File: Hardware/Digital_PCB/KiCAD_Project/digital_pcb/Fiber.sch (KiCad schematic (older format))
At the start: 8 parts, among them Q1 MMBT3904, U6 SN74LVC1G17-EP

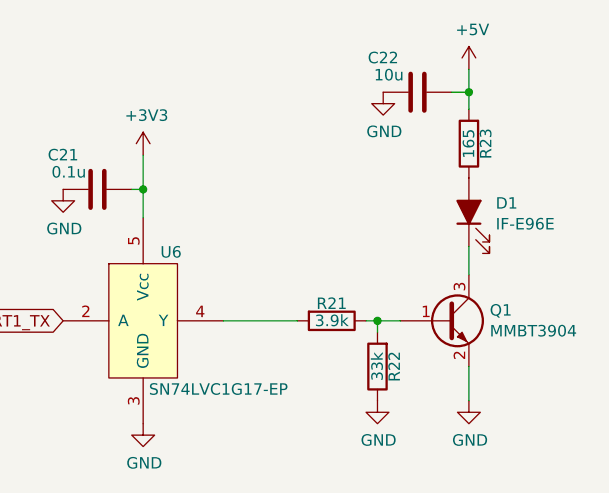
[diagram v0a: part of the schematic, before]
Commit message: Digital PCB Rev 1.0 complete.
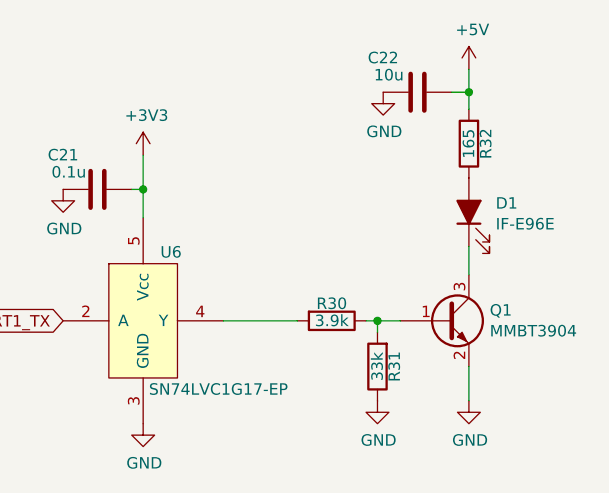
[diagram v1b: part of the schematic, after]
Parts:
- renumbered R21 to R30, R22 to R31, R23 to R32
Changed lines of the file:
@@
 Sheet 4 5
 Title "Digital Rotating Electronics - NSSL EFM"
-Date "2019-11-26"
+Date "2019-12-30"
 Rev "1.0"
 Comp "Leeman Geophysical LLC"
@@
 UART1_TX
 $Comp
-L Device:R R21
+L Device:R R30
 U 1 1 5DECF997
 P 6000 3750
-F 0 "R21" V 5925 3750 50  0000 C CNN
+F 0 "R30" V 5925 3750 50  0000 C CNN
 F 1 "3.9k" V 6000 3750 50  0000 C CNN
 F 2 "Resistors_SMD:R_0603_HandSoldering" V 5930 3750 50  0001 C CNN
@@
 $EndComp
 $Comp
-L Device:R R22
+L Device:R R31
 U 1 1 5DECFEA9
 P 6200 3950
-F 0 "R22" V 6125 3950 50  0000 C CNN
+F 0 "R31" V 6125 3950 50  0000 C CNN
 F 1 "33k" V 6200 3950 50  0000 C CNN
 F 2 "Resistors_SMD:R_0603_HandSoldering" V 6130 3950 50  0001 C CNN
@@
 	6200 3750 6300 3750
 $Comp
-L power:GND #PWR051
+L power:GND #PWR061
 U 1 1 5DED209E
 P 6200 4100
-F 0 "#PWR051" H 6200 3850 50  0001 C CNN
+F 0 "#PWR061" H 6200 3850 50  0001 C CNN
 F 1 "GND" H 6205 3927 50  0000 C CNN
 F 2 "" H 6200 4100 50  0001 C CNN
@@
 $EndComp
 $Comp
-L power:GND #PWR054
+L power:GND #PWR064
 U 1 1 5DED2797
 P 6600 4100
-F 0 "#PWR054" H 6600 3850 50  0001 C CNN
+F 0 "#PWR064" H 6600 3850 50  0001 C CNN
 F 1 "GND" H 6605 3927 50  0000 C CNN
 F 2 "" H 6600 4100 50  0001 C CNN
@@
 	6600 3425 6600 3550
 $Comp
-L Device:R R23
+L Device:R R32
 U 1 1 5DED4330
 P 6600 2975
-F 0 "R23" V 6525 2975 50  0000 C CNN
+F 0 "R32" V 6525 2975 50  0000 C CNN
 F 1 "165" V 6600 2975 50  0000 C CNN
 F 2 "Resistors_SMD:R_0603_HandSoldering" V 6530 2975 50  0001 C CNN
@@
 $EndComp
 $Comp
-L power:+5V #PWR053
+L power:+5V #PWR063
 U 1 1 5DED4F9E
 P 6600 2650
-F 0 "#PWR053" H 6600 2500 50  0001 C CNN
+F 0 "#PWR063" H 6600 2500 50  0001 C CNN
 F 1 "+5V" H 6615 2823 50  0000 C CNN
 F 2 "" H 6600 2650 50  0001 C CNN
@@
 	5525 3750 5850 3750
 $Comp
-L power:GND #PWR050
+L power:GND #PWR060
 U 1 1 5DED5B72
 P 5175 4200
-F 0 "#PWR050" H 5175 3950 50  0001 C CNN
+F 0 "#PWR060" H 5175 3950 50  0001 C CNN
 F 1 "GND" H 5180 4027 50  0000 C CNN
 F 2 "" H 5175 4200 50  0001 C CNN
@@
 $EndComp
 $Comp
-L power:+3V3 #PWR049
+L power:+3V3 #PWR059
 U 1 1 5DED600C
 P 5175 3025
-F 0 "#PWR049" H 5175 2875 50  0001 C CNN
+F 0 "#PWR059" H 5175 2875 50  0001 C CNN
 F 1 "+3V3" H 5190 3198 50  0000 C CNN
 F 2 "" H 5175 3025 50  0001 C CNN
@@
 Connection ~ 5175 3175
 $Comp
-L power:GND #PWR048
+L power:GND #PWR058
 U 1 1 5DED7C4C
 P 4825 3175
-F 0 "#PWR048" H 4825 2925 50  0001 C CNN
+F 0 "#PWR058" H 4825 2925 50  0001 C CNN
 F 1 "GND" H 4830 3002 50  0000 C CNN
 F 2 "" H 4825 3175 50  0001 C CNN
@@
 $EndComp
 $Comp
-L power:GND #PWR052
+L power:GND #PWR062
 U 1 1 5DED8B30
 P 6225 2750
-F 0 "#PWR052" H 6225 2500 50  0001 C CNN
+F 0 "#PWR062" H 6225 2500 50  0001 C CNN
 F 1 "GND" H 6230 2577 50  0000 C CNN
 F 2 "" H 6225 2750 50  0001 C CNN

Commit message: Debounce power switch with load switch and RC timer. Closes #1.
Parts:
- C22: footprint Capacitors_SMD:C_0603_HandSoldering -> Capacitor_SMD:C_0805_2012Metric_Pad1.15x1.40mm_HandSolder
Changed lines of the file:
@@
 F 0 "C22" V 6225 2600 50  0000 C CNN
 F 1 "10u" V 6300 2625 50  0000 C CNN
-F 2 "Capacitors_SMD:C_0603_HandSoldering" H 6413 2600 50  0001 C CNN
+F 2 "Capacitor_SMD:C_0805_2012Metric_Pad1.15x1.40mm_HandSolder" H 6413 2600 50  0001 C CNN
 F 3 "~" H 6375 2750 50  0001 C CNN
 F 4 "1-0000075" H 6375 2750 50  0001 C CNN "Internal Part Number"

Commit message: Update footprints for R32 and fix various small layout things and silk screen.
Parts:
- R32: footprint Resistors_SMD:R_0603_HandSoldering -> Resistor_SMD:R_1206_3216Metric_Pad1.42x1.75mm_HandSolder
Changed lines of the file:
@@
 F 0 "R32" V 6525 2975 50  0000 C CNN
 F 1 "165" V 6600 2975 50  0000 C CNN
-F 2 "Resistors_SMD:R_0603_HandSoldering" V 6530 2975 50  0001 C CNN
+F 2 "Resistor_SMD:R_1206_3216Metric_Pad1.42x1.75mm_HandSolder" V 6530 2975 50  0001 C CNN
 F 3 "~" H 6600 2975 50  0001 C CNN
 F 4 "1-0000469" H 6600 2975 50  0001 C CNN "Internal Part Number"

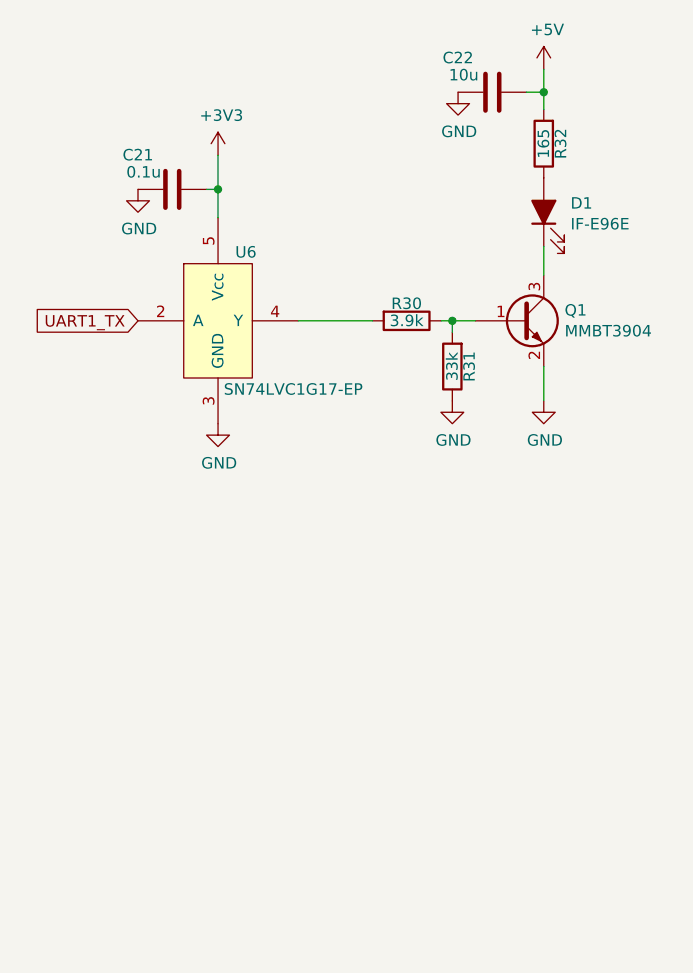
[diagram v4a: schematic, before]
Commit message: Update footprints
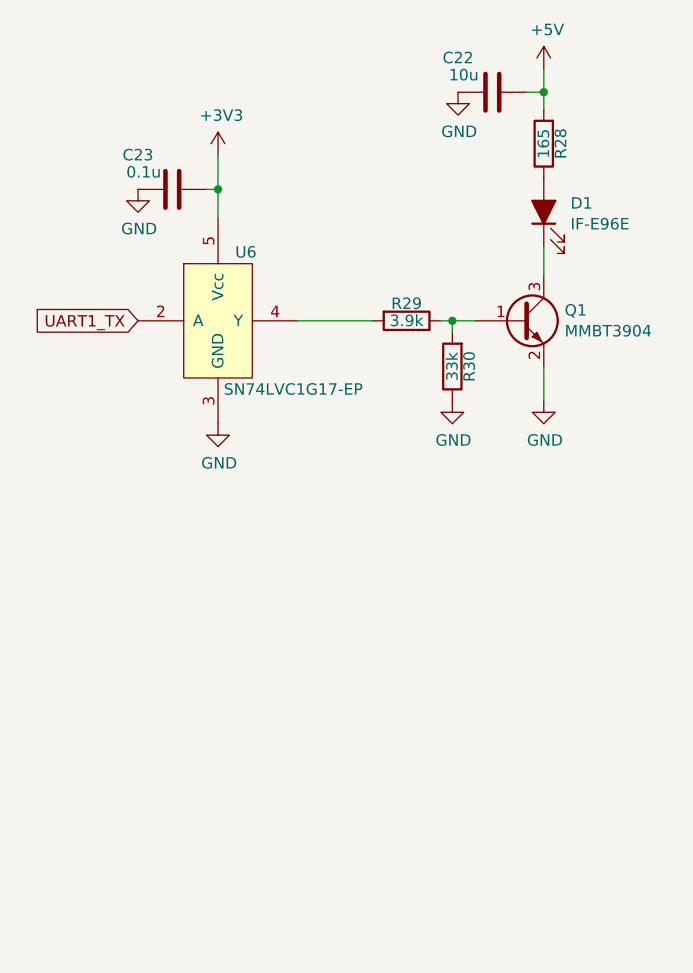
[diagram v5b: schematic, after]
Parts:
- C22: footprint Capacitor_SMD:C_0805_2012Metric_Pad1.15x1.40mm_HandSolder -> Capacitor_SMD:C_0805_2012Metric
- C23: renamed from C21; footprint Capacitors_SMD:C_0603_HandSoldering -> Capacitor_SMD:C_0603_1608Metric
- R28: renamed from R32; footprint Resistor_SMD:R_1206_3216Metric_Pad1.42x1.75mm_HandSolder -> Resistor_SMD:R_1206_3216Metric
- R29: renamed from R30; footprint Resistors_SMD:R_0603_HandSoldering -> Resistor_SMD:R_0603_1608Metric
- R30: renamed from R31; footprint Resistors_SMD:R_0603_HandSoldering -> Resistor_SMD:R_0603_1608Metric
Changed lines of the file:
@@
 UART1_TX
 $Comp
-L Device:R R30
+L Device:R R29
 U 1 1 5DECF997
 P 6000 3750
-F 0 "R30" V 5925 3750 50  0000 C CNN
+F 0 "R29" V 5925 3750 50  0000 C CNN
 F 1 "3.9k" V 6000 3750 50  0000 C CNN
-F 2 "Resistors_SMD:R_0603_HandSoldering" V 5930 3750 50  0001 C CNN
+F 2 "Resistor_SMD:R_0603_1608Metric" V 5930 3750 50  0001 C CNN
 F 3 "~" H 6000 3750 50  0001 C CNN
 F 4 "1-0000473" H 6000 3750 50  0001 C CNN "Internal Part Number"
@@
 $EndComp
 $Comp
-L Device:R R31
+L Device:R R30
 U 1 1 5DECFEA9
 P 6200 3950
-F 0 "R31" V 6125 3950 50  0000 C CNN
+F 0 "R30" V 6125 3950 50  0000 C CNN
 F 1 "33k" V 6200 3950 50  0000 C CNN
-F 2 "Resistors_SMD:R_0603_HandSoldering" V 6130 3950 50  0001 C CNN
+F 2 "Resistor_SMD:R_0603_1608Metric" V 6130 3950 50  0001 C CNN
 F 3 "~" H 6200 3950 50  0001 C CNN
 F 4 "1-0000472" H 6200 3950 50  0001 C CNN "Internal Part Number"
@@
 	6200 3750 6300 3750
 $Comp
-L power:GND #PWR061
+L power:GND #PWR063
 U 1 1 5DED209E
 P 6200 4100
-F 0 "#PWR061" H 6200 3850 50  0001 C CNN
+F 0 "#PWR063" H 6200 3850 50  0001 C CNN
 F 1 "GND" H 6205 3927 50  0000 C CNN
 F 2 "" H 6200 4100 50  0001 C CNN
@@
 	6600 3425 6600 3550
 $Comp
-L Device:R R32
+L Device:R R28
 U 1 1 5DED4330
 P 6600 2975
-F 0 "R32" V 6525 2975 50  0000 C CNN
+F 0 "R28" V 6525 2975 50  0000 C CNN
 F 1 "165" V 6600 2975 50  0000 C CNN
-F 2 "Resistor_SMD:R_1206_3216Metric_Pad1.42x1.75mm_HandSolder" V 6530 2975 50  0001 C CNN
+F 2 "Resistor_SMD:R_1206_3216Metric" V 6530 2975 50  0001 C CNN
 F 3 "~" H 6600 2975 50  0001 C CNN
 F 4 "1-0000469" H 6600 2975 50  0001 C CNN "Internal Part Number"
@@
 $EndComp
 $Comp
-L power:+5V #PWR063
+L power:+5V #PWR059
 U 1 1 5DED4F9E
 P 6600 2650
-F 0 "#PWR063" H 6600 2500 50  0001 C CNN
+F 0 "#PWR059" H 6600 2500 50  0001 C CNN
 F 1 "+5V" H 6615 2823 50  0000 C CNN
 F 2 "" H 6600 2650 50  0001 C CNN
@@
 	5525 3750 5850 3750
 $Comp
-L power:GND #PWR060
+L power:GND #PWR065
 U 1 1 5DED5B72
 P 5175 4200
-F 0 "#PWR060" H 5175 3950 50  0001 C CNN
+F 0 "#PWR065" H 5175 3950 50  0001 C CNN
 F 1 "GND" H 5180 4027 50  0000 C CNN
 F 2 "" H 5175 4200 50  0001 C CNN
@@
 $EndComp
 $Comp
-L power:+3V3 #PWR059
+L power:+3V3 #PWR061
 U 1 1 5DED600C
 P 5175 3025
-F 0 "#PWR059" H 5175 2875 50  0001 C CNN
+F 0 "#PWR061" H 5175 2875 50  0001 C CNN
 F 1 "+3V3" H 5190 3198 50  0000 C CNN
 F 2 "" H 5175 3025 50  0001 C CNN
@@
 P 4975 3175
 AR Path="/5DED751F" Ref="C?"  Part="1"
-AR Path="/5DE670A6/5DED751F" Ref="C21"  Part="1"
-F 0 "C21" V 4825 3025 50  0000 C CNN
+AR Path="/5DE670A6/5DED751F" Ref="C23"  Part="1"
+F 0 "C23" V 4825 3025 50  0000 C CNN
 F 1 "0.1u" V 4900 3050 50  0000 C CNN
-F 2 "Capacitors_SMD:C_0603_HandSoldering" H 5013 3025 50  0001 C CNN
+F 2 "Capacitor_SMD:C_0603_1608Metric" H 5013 3025 50  0001 C CNN
 F 3 "~" H 4975 3175 50  0001 C CNN
 F 4 "1-0000007" H 4975 3175 50  0001 C CNN "Internal Part Number"
@@
 Connection ~ 5175 3175
 $Comp
-L power:GND #PWR058
+L power:GND #PWR062
 U 1 1 5DED7C4C
 P 4825 3175
-F 0 "#PWR058" H 4825 2925 50  0001 C CNN
+F 0 "#PWR062" H 4825 2925 50  0001 C CNN
 F 1 "GND" H 4830 3002 50  0000 C CNN
 F 2 "" H 4825 3175 50  0001 C CNN
@@
 F 0 "C22" V 6225 2600 50  0000 C CNN
 F 1 "10u" V 6300 2625 50  0000 C CNN
-F 2 "Capacitor_SMD:C_0805_2012Metric_Pad1.15x1.40mm_HandSolder" H 6413 2600 50  0001 C CNN
+F 2 "Capacitor_SMD:C_0805_2012Metric" H 6413 2600 50  0001 C CNN
 F 3 "~" H 6375 2750 50  0001 C CNN
 F 4 "1-0000075" H 6375 2750 50  0001 C CNN "Internal Part Number"
@@
 $EndComp
 $Comp
-L power:GND #PWR062
+L power:GND #PWR060
 U 1 1 5DED8B30
 P 6225 2750
-F 0 "#PWR062" H 6225 2500 50  0001 C CNN
+F 0 "#PWR060" H 6225 2500 50  0001 C CNN
 F 1 "GND" H 6230 2577 50  0000 C CNN
 F 2 "" H 6225 2750 50  0001 C CNN

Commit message: Add activity LED and another IMU footprint. Closes #49 #45
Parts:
- added C43: 10u, Capacitor_SMD:C_0805_2012Metric, symbol Device:C
- added C44: 0.1u, Capacitor_SMD:C_0603_1608Metric, symbol Device:C
- added D2: 1-0000599, leds_0805:1-0000599, symbol leds_0805:1-0000599
- added Q2: 1-0000036, transistors:1-0000036, symbol transistors:1-0000036
- added R39: 165, Resistor_SMD:R_1206_3216Metric, symbol Device:R
- added R40: 3.9k, Resistor_SMD:R_0603_1608Metric, symbol Device:R
- added R41: 33k, Resistor_SMD:R_0603_1608Metric, symbol Device:R
- added U13: SN74LVC1G17-EP, Package_TO_SOT_SMD:SOT-23-5_HandSoldering, symbol lib_sch:SN74LVC1G17-EP
- Q1: value MMBT3904 -> 1-0000036; footprint TO_SOT_Packages_SMD:SOT-23 -> transistors:1-0000036; symbol Transistor_BJT:MMBT3904 -> transistors:1-0000036; PValue (none) -> MMBT3904
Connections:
- net +3V3: now also C44.1, U13.5 (Vcc)
- net +5V: now also C43.1, R39.2
- net GND: now also C43.2, C44.2, Q2.2 (E), R41.1, U13.3 (GND)
- net UART1_TX: now also U13.2 (A)
- new net: R40.2, U13.4 (Y)
- new net: Q2.1 (B), R40.1, R41.2
- new net: D2.2 (A), R39.1
- new net: D2.1 (K), Q2.3 (C)
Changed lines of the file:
@@
 $EndComp
 $Comp
-L Transistor_BJT:MMBT3904 Q1
+L transistors:1-0000036 Q1
 U 1 1 5DED031F
 P 6500 3750
 F 0 "Q1" H 6691 3796 50  0000 L CNN
-F 1 "MMBT3904" H 6691 3705 50  0000 L CNN
-F 2 "TO_SOT_Packages_SMD:SOT-23" H 6700 3675 50  0001 L CIN
-F 3 "https://www.fairchildsemi.com/datasheets/2N/2N3904.pdf" H 6500 3750 50  0001 L CNN
+F 1 "1-0000036" H 6691 3705 50  0001 L CNN
+F 2 "transistors:1-0000036" H 6700 3675 50  0001 L CIN
+F 3 "~" H 6500 3750 50  0001 L CNN
 F 4 "1-0000036" H 6500 3750 50  0001 C CNN "Internal Part Number"
 F 5 "1" H 6500 3750 50  0001 C CNN "Populated"
+F 6 "MMBT3904" H 6900 3700 50  0000 C CNN "PValue"
 	1    6500 3750
 	1    0    0    -1
@@
 Wire Wire Line
 	6600 2750 6600 2825
+$Comp
+L lib_sch:SN74LVC1G17-EP U13
+U 1 1 621D4E88
+P 5225 5850
+F 0 "U13" H 5300 6150 50  0000 L CNN
+F 1 "SN74LVC1G17-EP" H 5250 5550 50  0000 L CNN
+F 2 "Package_TO_SOT_SMD:SOT-23-5_HandSoldering" H 5225 5850 50  0001 C CNN
+F 3 "" H 5225 5850 50  0001 C CNN
+F 4 "1-0000466" H 5225 5850 50  0001 C CNN "Internal Part Number"
+F 5 "1" H 5225 5850 50  0001 C CNN "Populated"
+	1    5225 5850
+	1    0    0    -1
+$EndComp
+Text GLabel 4875 5850 0    50   Input ~ 0
+UART1_TX
+$Comp
+L Device:R R40
+U 1 1 621D4E91
+P 6050 5850
+F 0 "R40" V 5975 5850 50  0000 C CNN
+F 1 "3.9k" V 6050 5850 50  0000 C CNN
+F 2 "Resistor_SMD:R_0603_1608Metric" V 5980 5850 50  0001 C CNN
+F 3 "~" H 6050 5850 50  0001 C CNN
+F 4 "1-0000473" H 6050 5850 50  0001 C CNN "Internal Part Number"
+F 5 "1" H 6050 5850 50  0001 C CNN "Populated"
+	1    6050 5850
+	0    1    1    0
+$EndComp
+$Comp
+L Device:R R41
+U 1 1 621D4E99
+P 6250 6050
+F 0 "R41" V 6175 6050 50  0000 C CNN
+F 1 "33k" V 6250 6050 50  0000 C CNN
+F 2 "Resistor_SMD:R_0603_1608Metric" V 6180 6050 50  0001 C CNN
+F 3 "~" H 6250 6050 50  0001 C CNN
+F 4 "1-0000472" H 6250 6050 50  0001 C CNN "Internal Part Number"
+F 5 "1" H 6250 6050 50  0001 C CNN "Populated"
+	1    6250 6050
+	-1   0    0    1
+$EndComp
+Wire Wire Line
+	6200 5850 6250 5850
+Wire Wire Line
+	6250 5900 6250 5850
+Connection ~ 6250 5850
+Wire Wire Line
+	6250 5850 6350 5850
+$Comp
+L power:GND #PWR099
+U 1 1 621D4EAB
+P 6250 6200
+F 0 "#PWR099" H 6250 5950 50  0001 C CNN
+F 1 "GND" H 6255 6027 50  0000 C CNN
+F 2 "" H 6250 6200 50  0001 C CNN
+F 3 "" H 6250 6200 50  0001 C CNN
+	1    6250 6200
+	1    0    0    -1
+$EndComp
+$Comp
+L power:GND #PWR0100
+U 1 1 621D4EB1
+P 6650 6200
+F 0 "#PWR0100" H 6650 5950 50  0001 C CNN
+F 1 "GND" H 6655 6027 50  0000 C CNN
+F 2 "" H 6650 6200 50  0001 C CNN
+F 3 "" H 6650 6200 50  0001 C CNN
+	1    6650 6200
+	1    0    0    -1
+$EndComp
+Wire Wire Line
+	6650 6200 6650 6050
+Wire Wire Line
+	6650 5525 6650 5650
+$Comp
+L Device:R R39
+U 1 1 621D4EC3
+P 6650 5075
+F 0 "R39" V 6575 5075 50  0000 C CNN
+F 1 "165" V 6650 5075 50  0000 C CNN
+F 2 "Resistor_SMD:R_1206_3216Metric" V 6580 5075 50  0001 C CNN
+F 3 "~" H 6650 5075 50  0001 C CNN
+F 4 "1-0000469" H 6650 5075 50  0001 C CNN "Internal Part Number"
+F 5 "1" H 6650 5075 50  0001 C CNN "Populated"
+	1    6650 5075
+	-1   0    0    1
+$EndComp
+$Comp
+L power:+5V #PWR095
+U 1 1 621D4EC9
+P 6650 4750
+F 0 "#PWR095" H 6650 4600 50  0001 C CNN
+F 1 "+5V" H 6665 4923 50  0000 C CNN
+F 2 "" H 6650 4750 50  0001 C CNN
+F 3 "" H 6650 4750 50  0001 C CNN
+	1    6650 4750
+	1    0    0    -1
+$EndComp
+Wire Wire Line
+	5575 5850 5900 5850
+$Comp
+L power:GND #PWR0108
+U 1 1 621D4ED0
+P 5225 6300
+F 0 "#PWR0108" H 5225 6050 50  0001 C CNN
+F 1 "GND" H 5230 6127 50  0000 C CNN
+F 2 "" H 5225 6300 50  0001 C CNN
+F 3 "" H 5225 6300 50  0001 C CNN
+	1    5225 6300
+	1    0    0    -1
+$EndComp
+$Comp
+L power:+3V3 #PWR097
+U 1 1 621D4ED6
+P 5225 5125
+F 0 "#PWR097" H 5225 4975 50  0001 C CNN
+F 1 "+3V3" H 5240 5298 50  0000 C CNN
+F 2 "" H 5225 5125 50  0001 C CNN
+F 3 "" H 5225 5125 50  0001 C CNN
+	1    5225 5125
+	1    0    0    -1
+$EndComp
+$Comp
+L Device:C C?
+U 1 1 621D4EDE
+P 5025 5275
+AR Path="/621D4EDE" Ref="C?"  Part="1"
+AR Path="/5DE670A6/621D4EDE" Ref="C44"  Part="1"
+F 0 "C44" V 4875 5125 50  0000 C CNN
+F 1 "0.1u" V 4950 5150 50  0000 C CNN
+F 2 "Capacitor_SMD:C_0603_1608Metric" H 5063 5125 50  0001 C CNN
+F 3 "~" H 5025 5275 50  0001 C CNN
+F 4 "1-0000007" H 5025 5275 50  0001 C CNN "Internal Part Number"
+F 5 "1" H 5025 5275 50  0001 C CNN "Populated"
+	1    5025 5275
+	0    1    1    0
+$EndComp
+Wire Wire Line
+	5175 5275 5225 5275
+Wire Wire Line
+	5225 5275 5225 5400
+Wire Wire Line
+	5225 5125 5225 5275
+Connection ~ 5225 5275
+$Comp
+L power:GND #PWR098
+U 1 1 621D4EE8
+P 4875 5275
+F 0 "#PWR098" H 4875 5025 50  0001 C CNN
+F 1 "GND" H 4880 5102 50  0000 C CNN
+F 2 "" H 4875 5275 50  0001 C CNN
+F 3 "" H 4875 5275 50  0001 C CNN
+	1    4875 5275
+	1    0    0    -1
+$EndComp
+$Comp
+L Device:C C?
+U 1 1 621D4EF0
+P 6425 4850
+AR Path="/621D4EF0" Ref="C?"  Part="1"
+AR Path="/5DE670A6/621D4EF0" Ref="C43"  Part="1"
+F 0 "C43" V 6275 4700 50  0000 C CNN
+F 1 "10u" V 6350 4725 50  0000 C CNN
+F 2 "Capacitor_SMD:C_0805_2012Metric" H 6463 4700 50  0001 C CNN
+F 3 "~" H 6425 4850 50  0001 C CNN
+F 4 "1-0000075" H 6425 4850 50  0001 C CNN "Internal Part Number"
+F 5 "1" H 6425 4850 50  0001 C CNN "Populated"
+	1    6425 4850
+	0    1    1    0
+$EndComp
+$Comp
+L power:GND #PWR096
+U 1 1 621D4EF6
+P 6275 4850
+F 0 "#PWR096" H 6275 4600 50  0001 C CNN
+F 1 "GND" H 6280 4677 50  0000 C CNN
+F 2 "" H 6275 4850 50  0001 C CNN
+F 3 "" H 6275 4850 50  0001 C CNN
+	1    6275 4850
+	1    0    0    -1
+$EndComp
+Wire Wire Line
+	6650 4750 6650 4850
+Wire Wire Line
+	6575 4850 6650 4850
+Connection ~ 6650 4850
+Wire Wire Line
+	6650 4850 6650 4925
+$Comp
+L leds_0805:1-0000599 D2
+U 1 1 621D57AD
+P 6650 5375
+F 0 "D2" V 6689 5258 50  0000 R CNN
+F 1 "1-0000599" H 6650 5275 50  0001 C CNN
+F 2 "leds_0805:1-0000599" H 6650 5375 50  0001 C CNN
+F 3 "~" H 6650 5375 50  0001 C CNN
+F 4 "1-0000599" H 6650 5375 50  0001 C CNN "Internal Part Number"
+F 5 "1" H 6650 5375 50  0001 C CNN "Populated"
+F 6 "Blue" V 6598 5258 50  0000 R CNN "PValue"
+	1    6650 5375
+	0    -1   -1   0
+$EndComp
+$Comp
+L transistors:1-0000036 Q2
+U 1 1 621D7E7F
+P 6550 5850
+F 0 "Q2" H 6741 5896 50  0000 L CNN
+F 1 "1-0000036" H 6741 5805 50  0001 L CNN
+F 2 "transistors:1-0000036" H 6750 5775 50  0001 L CIN
+F 3 "~" H 6550 5850 50  0001 L CNN
+F 4 "1-0000036" H 6550 5850 50  0001 C CNN "Internal Part Number"
+F 5 "1" H 6550 5850 50  0001 C CNN "Populated"
+F 6 "MMBT3904" H 6950 5800 50  0000 C CNN "PValue"
+	1    6550 5850
+	1    0    0    -1
+$EndComp
 $EndSCHEMATC
